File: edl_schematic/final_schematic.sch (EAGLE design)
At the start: 290 parts, among them IC1 FT232RL, IC10 TL084D, IC11 TL084D, IC12 TL084D, IC13 TL084D, IC14 TL084D, IC15 TL084D, IC16 TL084D, IC17 TL084D, IC18 TL084D, IC19 TL084D, IC2 TL084D, IC20 TL084D, IC21 TL084D, IC22 TL084D, IC23 TL084D, IC24 TL084D, IC3 TL084D, IC4 TPS77333, IC6 7812TV, IC8 TL084D, IC9 TL084D, Q1 BC558B, U1 TMS320F28069_PN_80, U3 TLV5610_DW_20, U4 MAX395EWG, U6 MAX395EWG, U7 MAX395EWG

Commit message: small schematic added
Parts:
- removed R1, R197: (no value), SparkFun-Resistors:RESISTOR1206
- added JP19, JP20, JP21, JP22: (no value), jumper:JP4E
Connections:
- removed net A3Q\: U4.COM1
- removed net DTR_OUT: Q1.C, R1.2, R197.2
- new net INTEG_IN11: JP22.1, R144.1, R145.1
- new net INTEG_IN22: JP22.2, R155.1, R156.1
- new net INTEG_IN33: JP22.3, R151.1, R152.1
- new net INTEG_IN44: JP22.4, R153.1, R154.1
- new net INTEG_IN55: JP21.1, R161.1, R162.1
- new net INTEG_IN66: JP21.2, R167.1, R168.1
- new net INTEG_IN77: JP21.3, R163.1, R164.1
- new net INTEG_IN88: JP21.4, R165.1, R166.1
- net 3V3: now also IC4.!RESET, IC4.FB/SENSE; no longer Q1.E
- net A1P: now also U4.COM1; no longer U4.NO0
- net A1Q: now also U4.NO1; no longer U4.COM0
- net A3P: now also R155.2, U4.NO0; no longer R151.2, U4.NO1
- net A3Q: now also C38.2, IC23B.-IN, R140.1, R156.2, U4.COM0; no longer C36.2, IC23C.-IN, R139.1, R152.2
- net A5P: now also R151.2, U4.COM3; no longer R155.2, U4.NO2
- net A5Q: now also C36.2, IC23C.-IN, R139.1, R152.2, U4.NO3; no longer C38.2, IC23B.-IN, R140.1, R156.2, U4.COM2
- net A7P: now also U4.NO2; no longer U4.NO3
- net A7Q: now also U4.COM2; no longer U4.COM3
- net B1P: now also U4.NO7; no longer U4.NO4
- net B1Q: now also U4.COM7; no longer U4.COM4
- net B3P: now also R167.2, U4.COM6; no longer R163.2, U4.NO5
- net B3Q: now also C42.2, IC24B.-IN, R158.1, R168.2, U4.NO6; no longer C40.2, IC24C.-IN, R157.1, R164.2, U4.COM5
- net B5P: now also R163.2, U4.NO5; no longer R167.2, U4.NO6
- net B5Q: now also C40.2, IC24C.-IN, R157.1, R164.2, U4.COM5; no longer C42.2, IC24B.-IN, R158.1, R168.2, U4.COM6
- net B7P: now also U4.COM4; no longer U4.NO7
- net B7Q: now also U4.NO4; no longer U4.COM7
- net GND: now also IC4.!EN, Q1.C; no longer R197.1
- net INTEG_IN1: now also JP19.4; no longer R144.1, R145.1
- net INTEG_IN2: now also JP19.3; no longer R155.1, R156.1
- net INTEG_IN3: now also JP19.2; no longer R151.1, R152.1
- net INTEG_IN4: now also JP19.1; no longer R153.1, R154.1
- net INTEG_IN5: now also JP20.4; no longer R161.1, R162.1
- net INTEG_IN6: now also JP20.3; no longer R167.1, R168.1
- net INTEG_IN7: now also JP20.2; no longer R163.1, R164.1
- net INTEG_IN8: now also JP20.1; no longer R165.1, R166.1
- net RST_OUT: now also Q1.E; no longer R1.1

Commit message: Small board done except power and switch
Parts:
- removed IC10, IC11, IC12, IC13, IC2, IC8, IC9: TL084D, linear:TL084D
- removed R12: (no value), resistor:R-US_0207/7
- removed R18, R19, R20, R21, R22, R23, R24, R25, R35, R36, R37, R38, R39, R40, R41, R42, R43, R44, R45, R46, R47, R48, R49, R50, R51, R52, R53, R54, R55, R56, R57, R58, R59, R60, R61, R62, R63, R64, R65, R66, R67, R68, R69, R70, R71, R72, R73, R74, R75, R76, R77, R78, R79, R80, R81, R82, R83, R84, R85, R86, R87, R88: (no value), rcl:R-US_R1206
- added IC25, IC26, IC27, IC28, IC29, IC30, IC5: TL084D, linear:TL084D
- added JP24, JP25: (no value), jumper:JP4E
- added R1, R14, R197, R198, R199, R200, R201, R202, R203, R204, R205, R206, R207, R208, R209, R210, R211, R212, R213, R214, R215, R216, R217, R218, R219, R220, R221, R222, R223, R224, R225, R226, R227, R228, R229, R230, R231, R232, R233, R234, R235, R236, R237, R238, R239, R240, R241, R242, R243, R244, R245, R246, R247, R248, R249, R250, R251, R252, R253, R254, R255, R5, R6: (no value), rcl:R-US_R1206
- IC3: SPICEPREFIX (none) -> B
- R10, R11, R8, R9: device resistor:R-US_0207/7 -> rcl:R-US_R1206
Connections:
- removed net +3.3V: R104.1, R110.1, R116.1, R122.1, R128.1, R134.1, R22.1, R31.1, R40.1, R49.1, R58.1, R67.1, R76.1, R85.1, R92.1, R98.1
- removed net 5V: U6.!RESET, U6.V+, U7.!RESET, U7.V+
- removed net N$22: IC2A.-IN, R17.2, R18.1
- removed net N$24: IC2A.OUT, R18.2, R19.1
- removed net N$25: IC2C.-IN, R19.2, R20.1
- removed net N$27: IC2C.OUT, R20.2, R21.1
- removed net N$29: IC2B.OUT, R23.1, R25.2
- removed net N$34: IC2D.-IN, R23.2, R24.1
- removed net N$35: IC2B.-IN, R21.2, R22.2, R25.1
- removed net N$44: IC8A.-IN, R35.2, R36.1
- removed net N$45: IC8A.OUT, R36.2, R37.1
- removed net N$46: IC8C.-IN, R37.2, R38.1
- removed net N$47: IC8C.OUT, R38.2, R39.1
- removed net N$48: IC8B.OUT, R41.1, R43.2
- removed net N$50: IC8D.-IN, R41.2, R42.1
- removed net N$51: IC8B.-IN, R39.2, R40.2, R43.1
- removed net N$52: IC9A.-IN, R44.2, R45.1
- removed net N$53: IC9A.OUT, R45.2, R46.1
- removed net N$54: IC9C.-IN, R46.2, R47.1
- removed net N$55: IC9C.OUT, R47.2, R48.1
- removed net N$56: IC9B.OUT, R50.1, R52.2
- removed net N$58: IC9D.-IN, R50.2, R51.1
- removed net N$59: IC9B.-IN, R48.2, R49.2, R52.1
- removed net N$60: IC10A.-IN, R53.2, R54.1
- removed net N$61: IC10A.OUT, R54.2, R55.1
- removed net N$62: IC10C.-IN, R55.2, R56.1
- removed net N$63: IC10C.OUT, R56.2, R57.1
- removed net N$64: IC10B.OUT, R59.1, R61.2
- removed net N$66: IC10D.-IN, R59.2, R60.1
- removed net N$67: IC10B.-IN, R57.2, R58.2, R61.1
- removed net N$68: IC11A.-IN, R62.2, R63.1
- removed net N$69: IC11A.OUT, R63.2, R64.1
- removed net N$70: IC11C.-IN, R64.2, R65.1
- removed net N$71: IC11C.OUT, R65.2, R66.1
- removed net N$72: IC11B.OUT, R68.1, R70.2
- removed net N$74: IC11D.-IN, R68.2, R69.1
- removed net N$75: IC11B.-IN, R66.2, R67.2, R70.1
- removed net N$76: IC12A.-IN, R71.2, R72.1
- removed net N$77: IC12A.OUT, R72.2, R73.1
- removed net N$78: IC12C.-IN, R73.2, R74.1
- removed net N$79: IC12C.OUT, R74.2, R75.1
- removed net N$80: IC12B.OUT, R77.1, R79.2
- removed net N$82: IC12D.-IN, R77.2, R78.1
- removed net N$83: IC12B.-IN, R75.2, R76.2, R79.1
- removed net N$84: IC13A.-IN, R80.2, R81.1
- removed net N$85: IC13A.OUT, R81.2, R82.1
- removed net N$86: IC13C.-IN, R82.2, R83.1
- removed net N$87: IC13C.OUT, R83.2, R84.1
- removed net N$88: IC13B.OUT, R86.1, R88.2
- removed net N$90: IC13D.-IN, R86.2, R87.1
- removed net N$91: IC13B.-IN, R84.2, R85.2, R88.1
- new net N$134: IC5A.OUT, R5.2, R6.1
- new net N$135: IC3B.OUT, R29.2, R30.1
- new net N$137: IC5B.-IN, R14.1, R6.2
- new net N$138: IC5C.OUT, R199.1, R201.2
- new net N$139: IC5D.-IN, R199.2, R200.1
- new net N$140: IC5C.-IN, R197.2, R198.2, R201.1
- new net N$141: IC5B.OUT, R14.2, R197.1
- new net N$142: IC25A.-IN, R202.2, R203.1
- new net N$143: IC25A.OUT, R203.2, R204.1
- new net N$144: IC25B.-IN, R204.2, R205.1
- new net N$145: IC25C.OUT, R208.1, R210.2
- new net N$146: IC25D.-IN, R208.2, R209.1
- new net N$147: IC25C.-IN, R206.2, R207.2, R210.1
- new net N$148: IC25B.OUT, R205.2, R206.1
- new net N$149: IC26A.-IN, R211.2, R212.1
- new net N$150: IC26A.OUT, R212.2, R213.1
- new net N$151: IC26B.-IN, R213.2, R214.1
- new net N$152: IC26C.OUT, R217.1, R219.2
- new net N$153: IC26D.-IN, R217.2, R218.1
- new net N$154: IC26C.-IN, R215.2, R216.2, R219.1
- new net N$155: IC26B.OUT, R214.2, R215.1
- new net N$156: IC27A.-IN, R220.2, R221.1
- new net N$157: IC27A.OUT, R221.2, R222.1
- new net N$158: IC27B.-IN, R222.2, R223.1
- new net N$159: IC27C.OUT, R226.1, R228.2
- new net N$160: IC27D.-IN, R226.2, R227.1
- new net N$161: IC27C.-IN, R224.2, R225.2, R228.1
- new net N$162: IC27B.OUT, R223.2, R224.1
- new net N$163: IC28A.-IN, R229.2, R230.1
- new net N$164: IC28A.OUT, R230.2, R231.1
- new net N$165: IC28B.-IN, R231.2, R232.1
- new net N$166: IC28C.OUT, R235.1, R237.2
- new net N$167: IC28D.-IN, R235.2, R236.1
- new net N$168: IC28C.-IN, R233.2, R234.2, R237.1
- new net N$169: IC28B.OUT, R232.2, R233.1
- new net N$170: IC29A.-IN, R238.2, R239.1
- new net N$171: IC29A.OUT, R239.2, R240.1
- new net N$172: IC29B.-IN, R240.2, R241.1
- new net N$173: IC29C.OUT, R244.1, R246.2
- new net N$174: IC29D.-IN, R244.2, R245.1
- new net N$175: IC29C.-IN, R242.2, R243.2, R246.1
- new net N$176: IC29B.OUT, R241.2, R242.1
- new net N$177: IC30A.-IN, R247.2, R248.1
- new net N$178: IC30A.OUT, R248.2, R249.1
- new net N$179: IC30B.-IN, R249.2, R250.1
- new net N$180: IC30C.OUT, R253.1, R255.2
- new net N$181: IC30D.-IN, R253.2, R254.1
- new net N$182: IC30C.-IN, R251.2, R252.2, R255.1
- new net N$183: IC30B.OUT, R250.2, R251.1
- net +12V: now also IC25P.V+, IC26P.V+, IC27P.V+, IC28P.V+, IC29P.V+, IC30P.V+, IC5P.V+, U4.!RESET, U4.V+, U6.!RESET, U6.V+, U7.!RESET, U7.V+; no longer IC10P.V+, IC11P.V+, IC12P.V+, IC13P.V+, IC2P.V+, IC8P.V+, IC9P.V+
- net -12V: now also IC25P.V-, IC26P.V-, IC27P.V-, IC28P.V-, IC29P.V-, IC30P.V-, IC5P.V-; no longer IC10P.V-, IC11P.V-, IC12P.V-, IC13P.V-, IC2P.V-, IC8P.V-, IC9P.V-
- net 3V3: now also R104.1, R110.1, R116.1, R122.1, R128.1, R134.1, R198.1, R207.1, R216.1, R225.1, R234.1, R243.1, R252.1, R31.1, R9.2, R92.1, R98.1; no longer R12.2, U4.!RESET, U4.V+
- net ADC_IN1: now also IC30D.OUT, JP25.4, R254.2; no longer IC3D.OUT, JP18.1, R33.2
- net ADC_IN2: now also IC28D.OUT, JP25.3, R236.2; no longer IC11D.OUT, JP18.3, R69.2
- net ADC_IN3: now also IC26D.OUT, JP25.2, R218.2; no longer IC8D.OUT, JP18.5, R42.2
- net ADC_IN4: now also IC25D.OUT, JP25.1, R209.2; no longer IC12D.OUT, JP18.7, R78.2
- net ADC_IN5: now also IC3D.OUT, JP24.1, R33.2; no longer IC9D.OUT, JP18.9, R51.2
- net ADC_IN6: now also IC5D.OUT, JP24.2, R200.2; no longer IC2D.OUT, JP18.11, R24.2
- net ADC_IN7: now also IC27D.OUT, JP24.3, R227.2; no longer IC10D.OUT, JP18.13, R60.2
- net ADC_IN8: now also IC29D.OUT, JP24.4, R245.2; no longer IC13D.OUT, JP18.15, R87.2
- net ADC_ORG1: now also JP18.6; no longer JP18.2
- net ADC_ORG2: now also JP18.8; no longer JP18.4
- net ADC_ORG3: now also JP18.10; no longer JP18.6
- net ADC_ORG4: now also JP18.12; no longer JP18.8
- net ADC_ORG5: now also JP18.14; no longer JP18.10
- net ADC_ORG6: now also JP18.16; no longer JP18.12
- net ADC_ORG7: now also JP18.4; no longer JP18.14
- net ADC_ORG8: now also JP18.2; no longer JP18.16
- net C1Q: now also U6.COM3, U6.NO0; no longer JP12.6, U6.COM0, U6.COM1
- net C3Q: now also U6.COM1, U6.NO2; no longer JP12.8, U6.COM2, U6.COM3
- net C5Q: now also JP12.10, JP12.9
- net C7Q: now also JP12.5, JP12.6
- net COMP2: now also R17.2; no longer R8.2
- net D1Q: now also U7.COM3, U7.NO0; no longer JP12.5, U7.COM0, U7.COM1
- net D3Q: now also U7.COM1, U7.NO2; no longer JP12.7, U7.COM2, U7.COM3
- net FORCE1: now also JP9.12; no longer JP9.11
- net FORCE2: now also JP9.14; no longer JP9.12
- net FORCE3: now also JP9.11; no longer JP9.13
- net FORCE4: now also JP9.13; no longer JP9.14
- net GND: now also IC25A.+IN, IC25B.+IN, IC25C.+IN, IC25D.+IN, IC26A.+IN, IC26B.+IN, IC26C.+IN, IC26D.+IN, IC27A.+IN, IC27B.+IN, IC27C.+IN, IC27D.+IN, IC28A.+IN, IC28B.+IN, IC28C.+IN, IC28D.+IN, IC29A.+IN, IC29B.+IN, IC29C.+IN, IC29D.+IN, IC30A.+IN, IC30B.+IN, IC30C.+IN, IC30D.+IN, IC5A.+IN, IC5B.+IN, IC5C.+IN, IC5D.+IN, R17.1; no longer IC10A.+IN, IC10B.+IN, IC10C.+IN, IC10D.+IN, IC11A.+IN, IC11B.+IN, IC11C.+IN, IC11D.+IN, IC12A.+IN, IC12B.+IN, IC12C.+IN, IC12D.+IN, IC13A.+IN, IC13B.+IN, IC13C.+IN, IC13D.+IN, IC2A.+IN, IC2B.+IN, IC2C.+IN, IC2D.+IN, IC8A.+IN, IC8B.+IN, IC8C.+IN, IC8D.+IN, IC9A.+IN, IC9B.+IN, IC9C.+IN, IC9D.+IN, JP12.13, JP12.14, R9.1
- net LIN_OUT1: now also JP12.13; no longer JP12.10
- net LIN_OUT1_SW: now also JP12.14; no longer JP12.12
- net LIN_OUT2: now also JP12.1; no longer JP12.9
- net LIN_OUT2_SW: now also JP12.2; no longer JP12.11
- net N$19: now also R9.1; no longer R11.1
- net N$21: now also R11.1; no longer R12.1
- net N$38: now also IC3B.-IN; no longer IC3C.-IN
- net N$39: now also IC5A.-IN, R1.2, R5.1; no longer IC3C.OUT, R29.2, R30.1
- net N$40: now also IC3C.OUT; no longer IC3B.OUT
- net N$43: now also IC3C.-IN; no longer IC3B.-IN
- net TDO: now also R10.2; no longer R9.2
- net TRST: now also R8.2; no longer R10.2
- net U1: now also JP12.11; no longer JP12.2
- net U2: now also JP12.3; no longer JP12.1
- net VIN1: now also R247.1; no longer R26.1, U6.NO0, U6.NO2
- net VIN1_INV: now also U6.COM2; no longer U6.NO1
- net VIN1_SW: now also JP12.12, U6.COM0, U6.NO1; no longer JP12.4
- net VIN2: now also JP15.3, R229.1; no longer JP15.2, R62.1, U7.NO0, U7.NO2
- net VIN2_INV: now also U7.COM0; no longer U7.NO3
- net VIN2_SW: now also JP12.4, U7.COM2, U7.NO3; no longer JP12.3
- net VIN3: now also JP15.5, R211.1; no longer JP15.3, R35.1
- net VIN4: now also JP15.7, R202.1; no longer JP15.4, R71.1
- net VIN5: now also JP15.2, R26.1; no longer JP15.5, R44.1
- net VIN6: now also JP15.4, R1.1; no longer JP15.6, R17.1
- net VIN7: now also JP15.6, R220.1; no longer JP15.7, R53.1
- net VIN8: now also R238.1; no longer R80.1
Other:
- moved on the sheet: IC3B, IC3C, R10, R11, R17, R8, R9

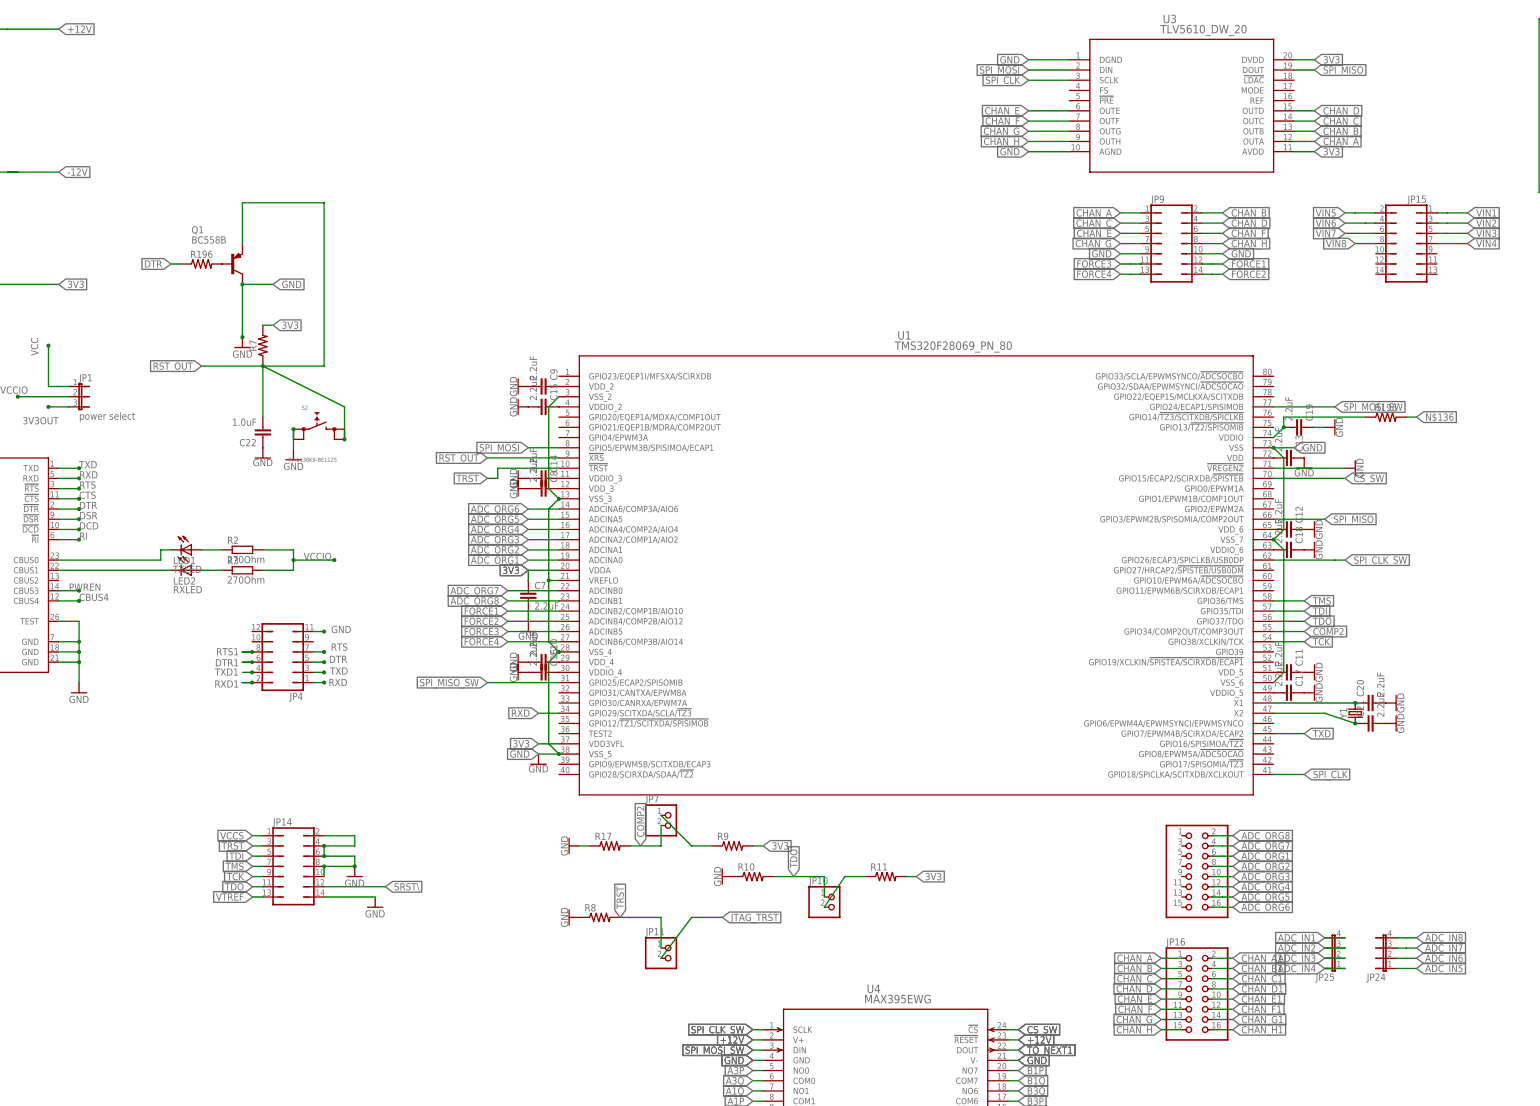
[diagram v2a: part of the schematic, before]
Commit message: layout done except drc
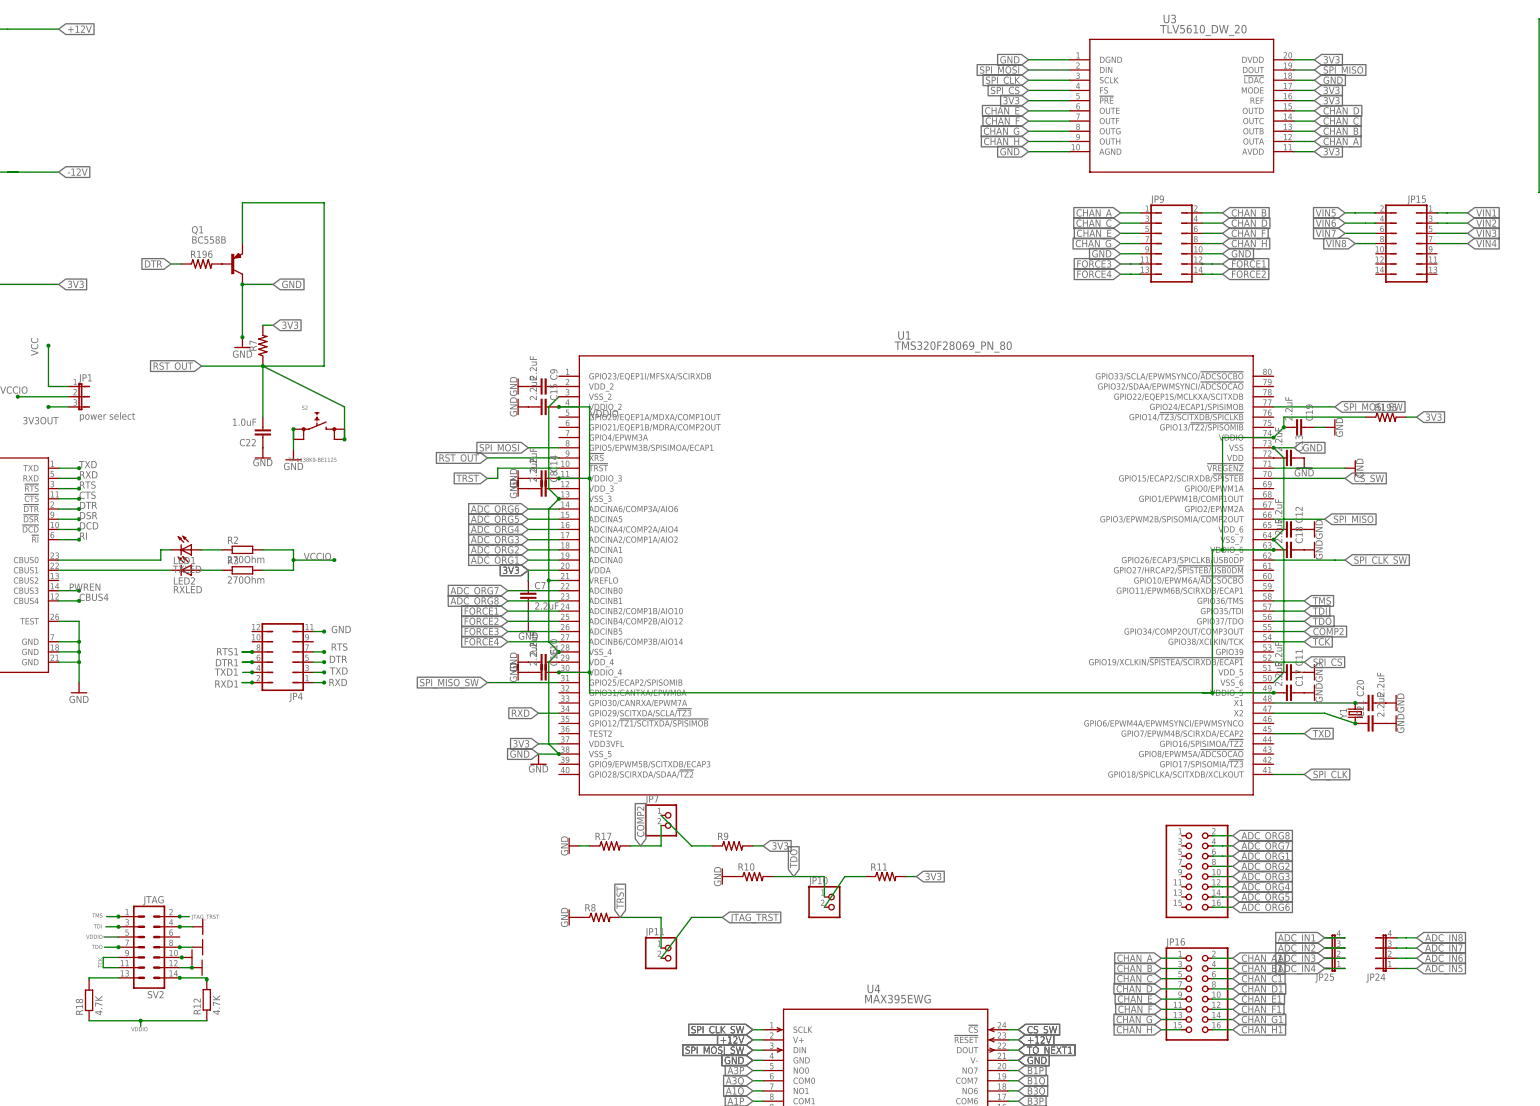
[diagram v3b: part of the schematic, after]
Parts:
- removed JP14: (no value), jumper:JP7Q
- added R12, R18: 4.7K, rcl:R-EU_M1206
- added SV2: JTAG, con-lstb:MA07-2
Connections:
- removed net N$12: C14.1, U1.VDDIO_3
- removed net N$13: C15.1, U1.VDDIO_2
- removed net N$136: R195.2
- removed net N$14: C16.1, U1.VDDIO_4
- removed net N$15: C17.2, U1.VDDIO_5
- removed net N$16: C18.2, U1.VDDIO_6
- removed net N$17: C19.2, R195.1, U1.VDDIO
- removed net SRST\: JP14.12
- removed net VCCS: JP14.1
- removed net VTREF: JP14.13
- new net N$22: R18.2, SV2.13
- new net N$24: R12.2, SV2.14
- new net SPI_CS: U1.GPIO19/XCLKIN/!SPISTEA/SCIRXDB/ECAP1, U3.FS
- new net VDDIO: C14.1, C15.1, C16.1, C17.2, C18.2, C19.2, R12.1, R18.1, R195.1, SV2.5, U1.VDDIO, U1.VDDIO_2, U1.VDDIO_3, U1.VDDIO_4, U1.VDDIO_5, U1.VDDIO_6
- net 3V3: now also R195.2, U3.!PRE, U3.MODE, U3.REF
- net GND: now also SV2.10, SV2.12, SV2.4, SV2.8, U3.!LDAC; no longer JP14.10, JP14.14, JP14.2, JP14.4, JP14.6, JP14.8
- net JTAG_TRST: now also SV2.2
- net TCK: now also SV2.11, SV2.9; no longer JP14.9
- net TDI: now also SV2.3; no longer JP14.5
- net TDO: now also SV2.7; no longer JP14.11
- net TMS: now also SV2.1; no longer JP14.7
- net TRST: no longer JP14.3
